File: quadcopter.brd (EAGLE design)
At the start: 203.5 x 203.5 mm, 76 parts, among them J1 AVR_SPI_PRG_6NS, U3 ATMEGA128RFA1

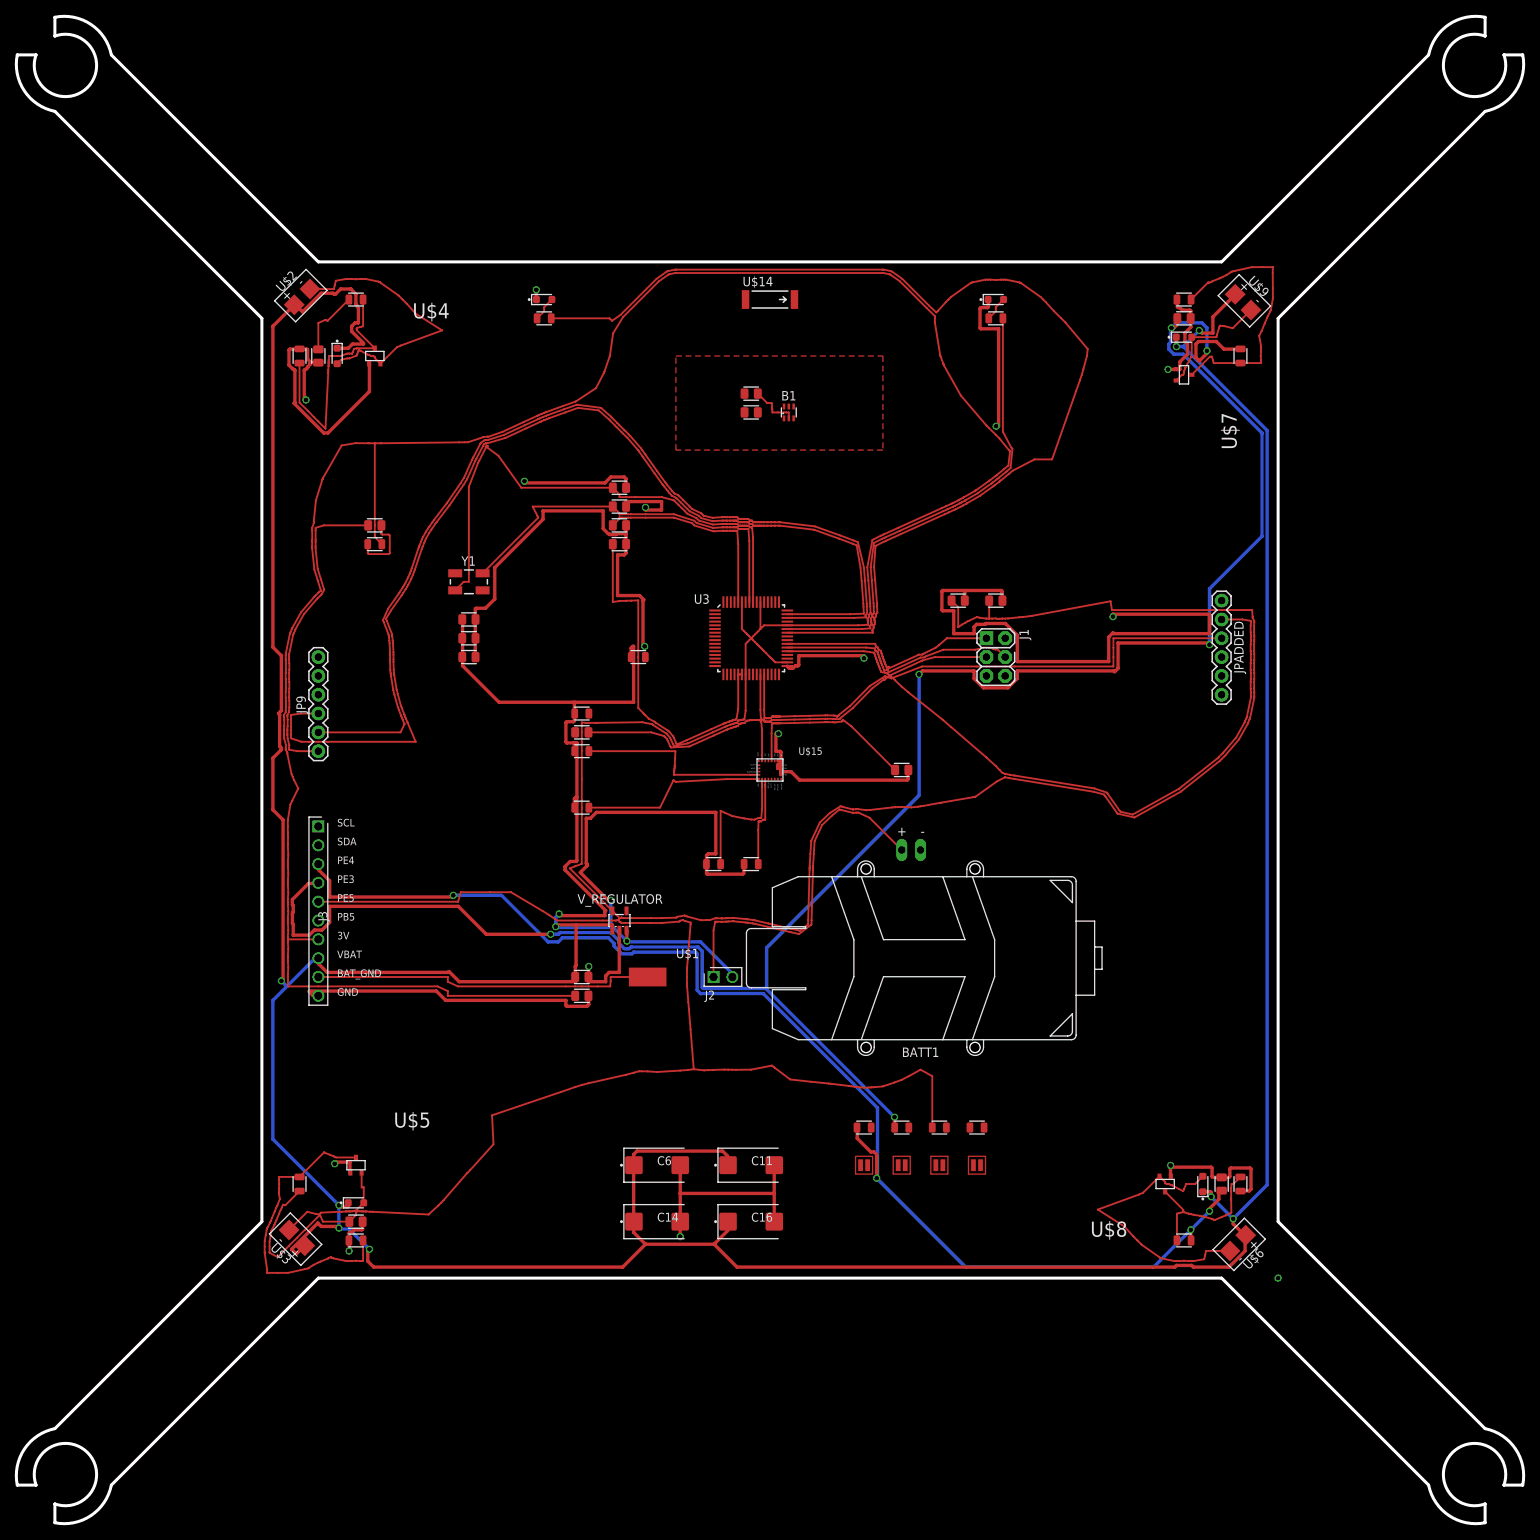
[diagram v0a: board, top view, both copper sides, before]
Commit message: made changes to schematic/board per the comments the prof made
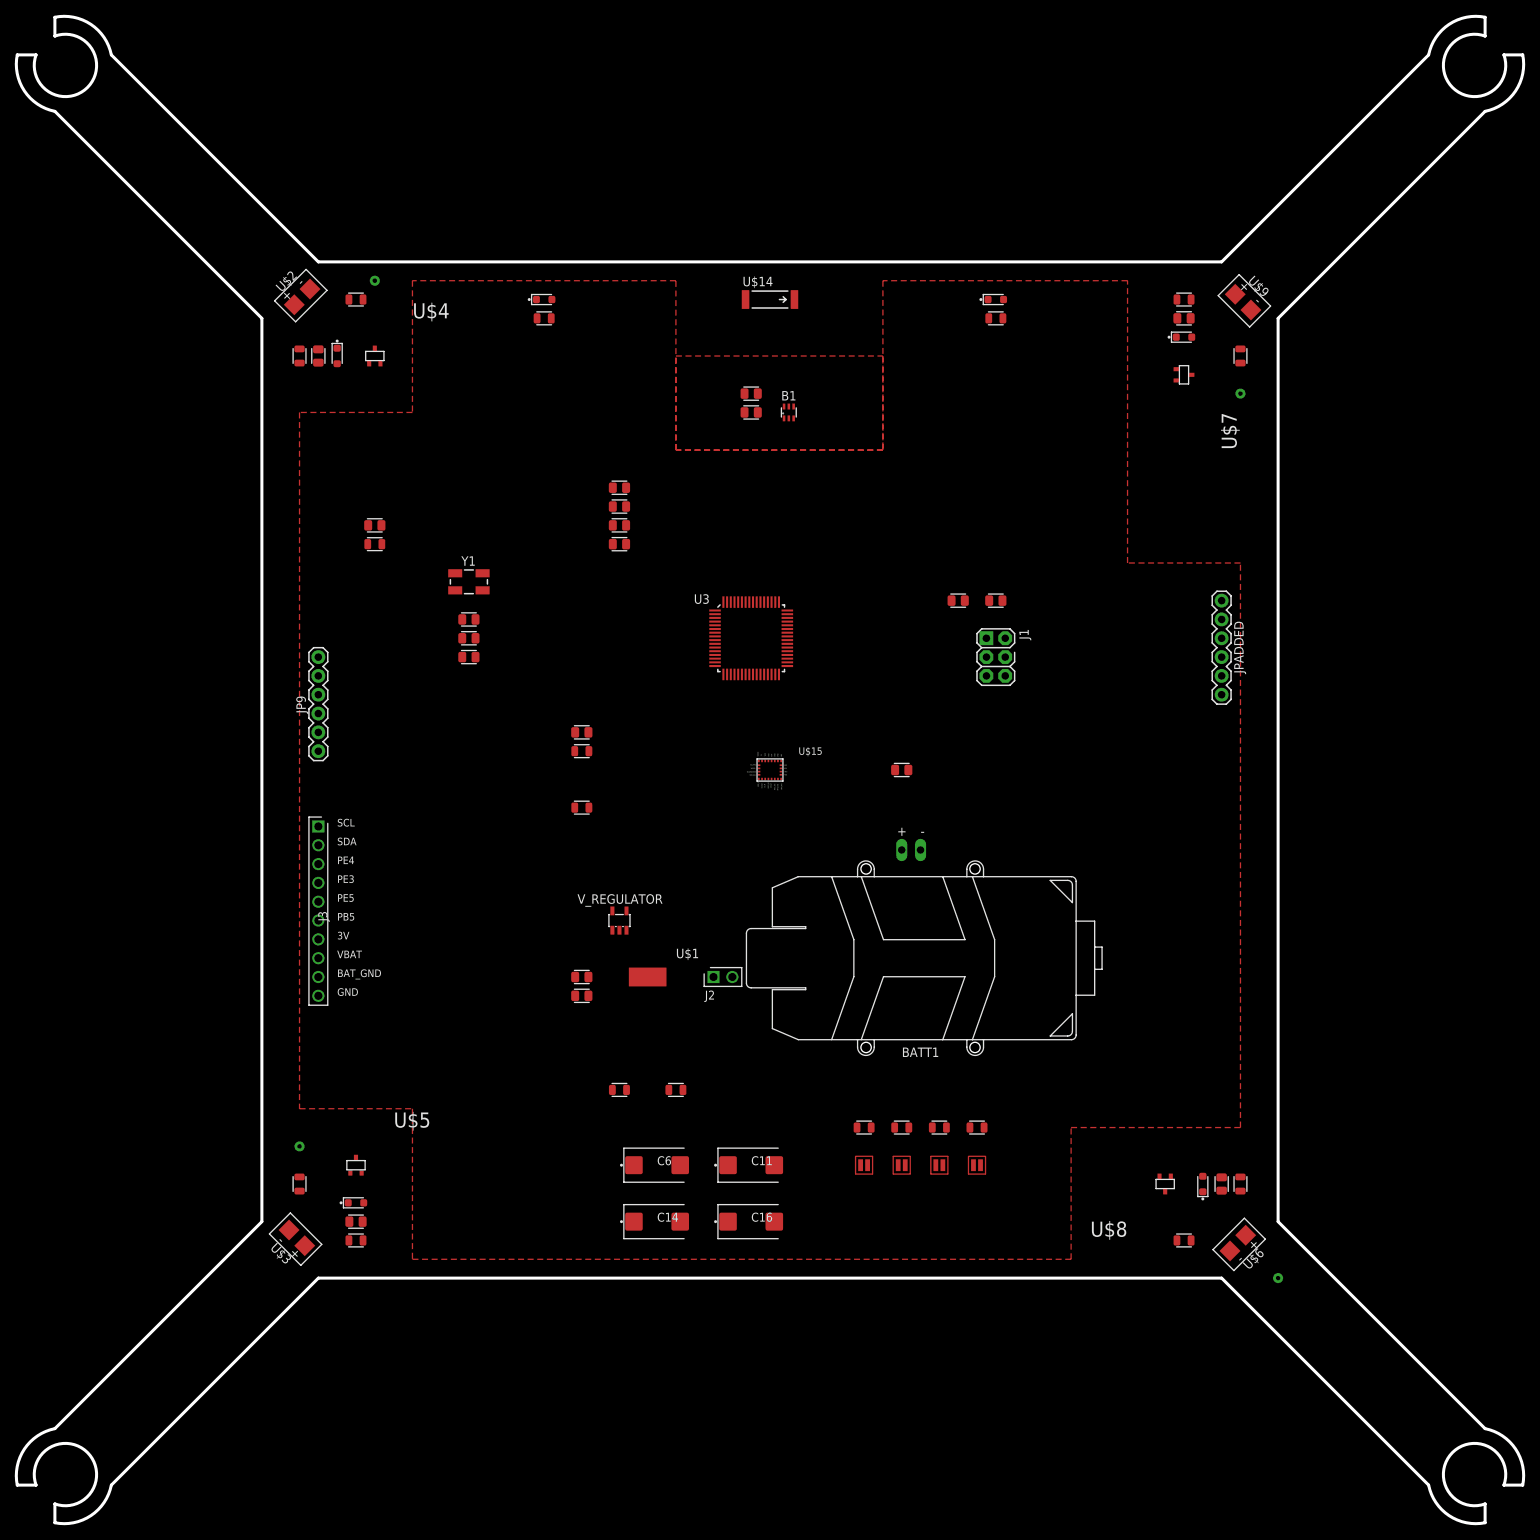
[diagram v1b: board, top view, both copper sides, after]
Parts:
- removed R20, R21: 10K, quadparts_prebuilt:RESC2012X60_HS
- C24: value 10nF -> 10uF
- moved R17 58.6 mm to (-12.7, -43.2)
- moved R16 51.1 mm to (-20.3, -43.2)
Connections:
- net BAT_GND: now also C11.2, C14.2, C16.2, C2.2, C27.2, C28.2, C3.2, C6.2
- net GND: no longer C11.2, C14.2, C16.2, C2.2, C27.2, C28.2, C3.2, C6.2
- net N$16: now also R17.2, U$15.P$2; no longer R20.2, U$15.P$7
- net N$17: now also R16.2, U$15.P$4; no longer R21.2, U$15.P$8
- net PE3: now also U3.49
- net PE4: now also U3.50
- net PE5: now also U3.51
- net SCL: no longer R16.2, U$15.P$2
- net SDA: no longer R17.2, U$15.P$4
- net VCC: now also U$15.P$7, U$15.P$8; no longer R20.1, R21.1
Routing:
- net VCC: track 701.5 -> 0.00 mm, vias 12 -> 0
- net 3V: track 550.1 -> 0.00 mm
- net GND: track 385.9 -> 0.00 mm, vias 15 -> 0
- net PE3: track 280.3 -> 0.00 mm, vias 6 -> 0
- net PE5: track 193.4 -> 0.00 mm
- net PE4: track 170.7 -> 0.00 mm, vias 4 -> 0
- net PB6: track 148.9 -> 0.00 mm
- net TX0: track 146.3 -> 0.00 mm
- net RX0: track 134.4 -> 0.00 mm
- net RX1: track 103.1 -> 0.00 mm
- net TX1: track 74.0 -> 0.00 mm
- net N$4: track 72.4 -> 0.00 mm
- net PB7: track 64.8 -> 0.00 mm
- net N$3: track 52.3 -> 0.00 mm
- net DVDD: track 48.4 -> 0.00 mm
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- added copper zone on layer 15, net ANTENA
- added copper zone on layer 1, net GND
- removed copper zone on layer 15, net N$23

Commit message: more changes made to board/schematic
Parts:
- removed C24: 10uF, quadparts_prebuilt:CAPC2012X140_HS
- removed C26: 100nF, quadparts_prebuilt:CAPC2012X140_HS
- removed R19: 10K, quadparts_prebuilt:RESC2012X60_HS
- added C22: 10uF, quadparts_prebuilt:CAPC2012X140_HS
- added C8: 0.1uF, quadparts_prebuilt:CAPC2012X140_HS
- moved BATT1 32.5 mm to (0.00, 0.00), flipped to the bottom
- moved U$10 30.9 mm to (27.9, -22.9)
- moved U$12 30.9 mm to (17.8, -22.9)
- moved U$13 30.9 mm to (33.0, -22.9)
- moved R1 30.9 mm to (27.9, -17.8)
- moved R15 30.9 mm to (33.0, -17.8)
- moved R8 30.9 mm to (17.8, -17.8)
- moved U$11 30.9 mm to (22.9, -22.9)
- moved R7 30.9 mm to (22.9, -17.8)
- moved J2 10.5 mm to (-5.08, -17.8)
- moved C3 5.08 mm to (-25.4, -22.9)
- moved C4 5.08 mm to (-25.4, -25.4)
- moved U$1 3.59 mm to (-12.7, -25.4)
- moved V_REGULATOR 3.59 mm to (-17.8, -17.8)
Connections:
- removed net N$15: R19.2, U$15.P$6
- removed net N$19: C26.1
- net BAT_GND: now also U$4.P$2, U$5.P$2, U$7.P$2, U$8.P$2; no longer C2.2, C27.2, C28.2
- net GND: now also C2.2, C22.2, C27.2, C28.2, C8.1; no longer C24.2, U$4.P$2, U$5.P$2, U$7.P$2, U$8.P$2
- net N$18: now also C8.2; no longer C26.2
- net N$20: now also C22.1; no longer C24.1
- net RX0: now also JP9.TXO; no longer JP9.RXI
- net RX1: now also JPADDED.TXO; no longer JPADDED.RXI
- net TX0: now also JP9.RXI; no longer JP9.TXO
- net TX1: now also JPADDED.RXI; no longer JPADDED.TXO
- net VCC: now also U$15.P$13, U$15.P$6; no longer R19.1

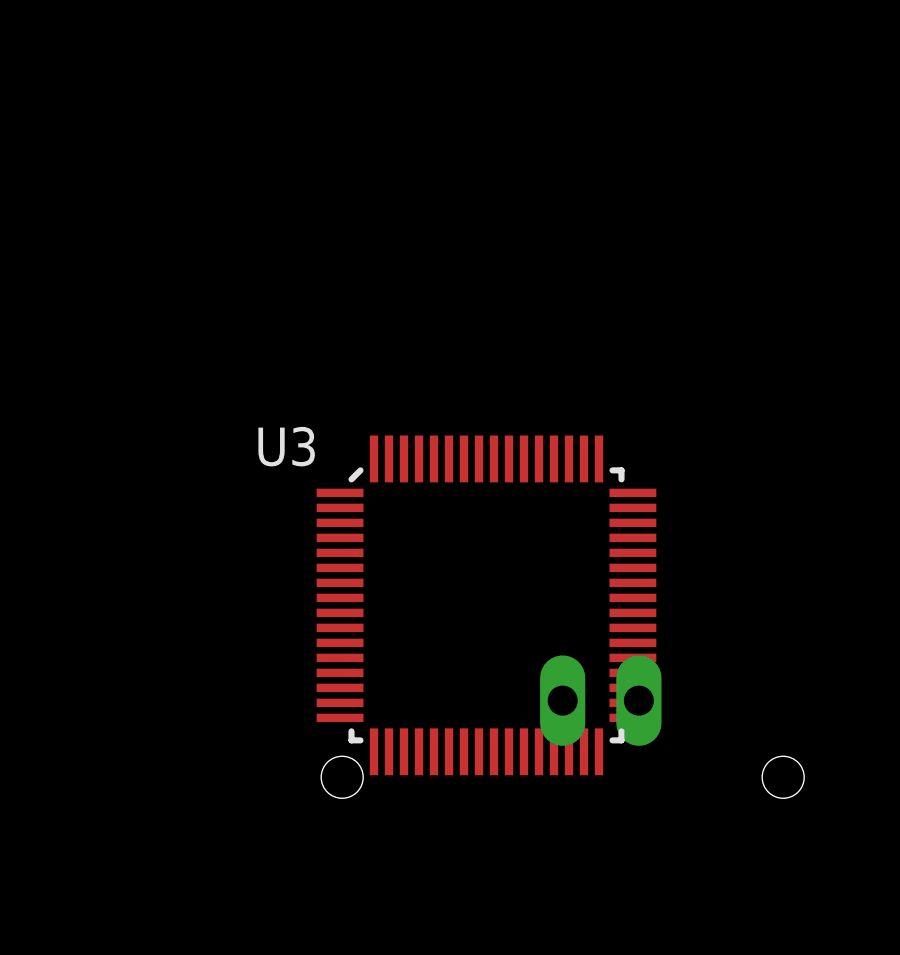
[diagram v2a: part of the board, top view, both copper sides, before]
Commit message: schematic and board no longer inconsistent
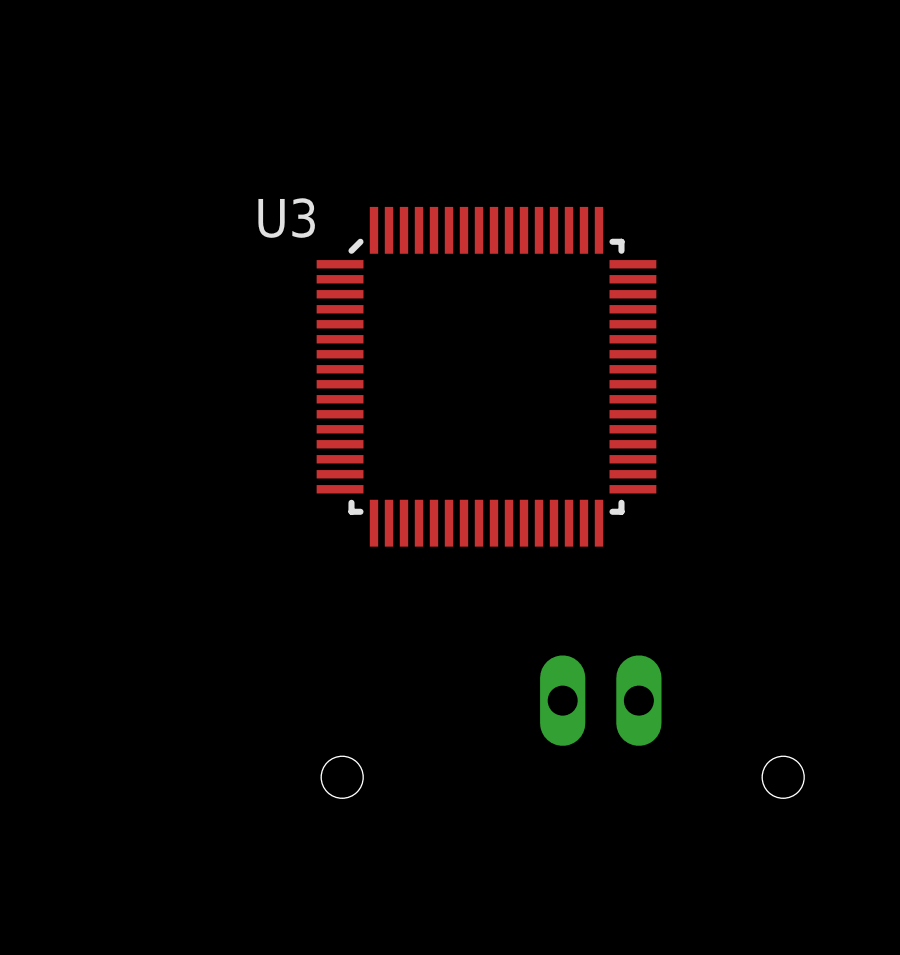
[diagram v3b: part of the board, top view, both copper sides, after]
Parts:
- moved U3 7.62 mm to (-2.54, 25.4)
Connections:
- removed net N$14: C10.1, R3.1
- removed net N$16: R17.2, U$15.P$2
- removed net N$17: R16.2, U$15.P$4
- net 3V: now also C2.1, C27.1, C28.1, R16.1, R17.1, R18.1, U$15.P$1, U$15.P$13, U$15.P$22, U$15.P$23, U$15.P$3, U$15.P$6, U$15.P$7, U$15.P$8
- net PB5: now also C10.1, R3.1
- net SCL: now also R17.2, U$15.P$2
- net SDA: now also R16.2, U$15.P$4
- net VCC: no longer C2.1, C27.1, C28.1, R16.1, R17.1, R18.1, U$15.P$1, U$15.P$13, U$15.P$22, U$15.P$23, U$15.P$3, U$15.P$6, U$15.P$7, U$15.P$8
